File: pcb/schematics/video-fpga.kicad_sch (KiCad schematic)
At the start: 58 parts, among them J5 Conn_01x06, J6 Conn_01x06, U4 LCMXO2-7000HC-4TG144C

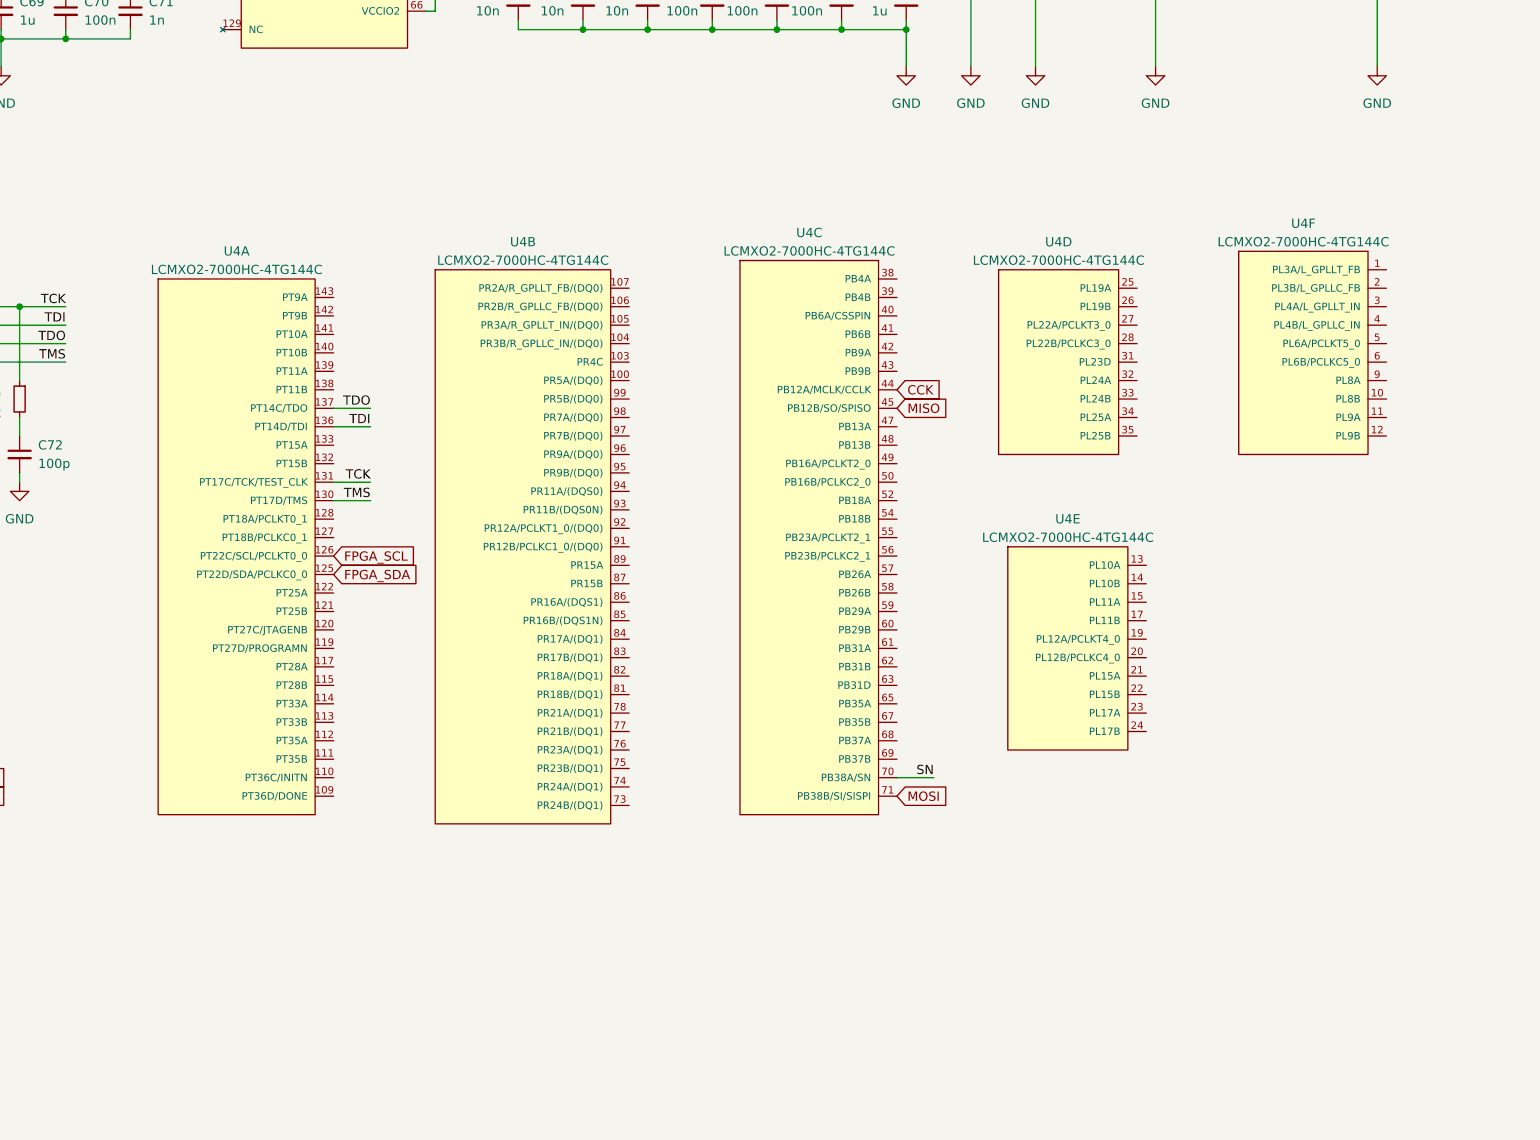
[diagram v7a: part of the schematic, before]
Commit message: add video controller oscillator
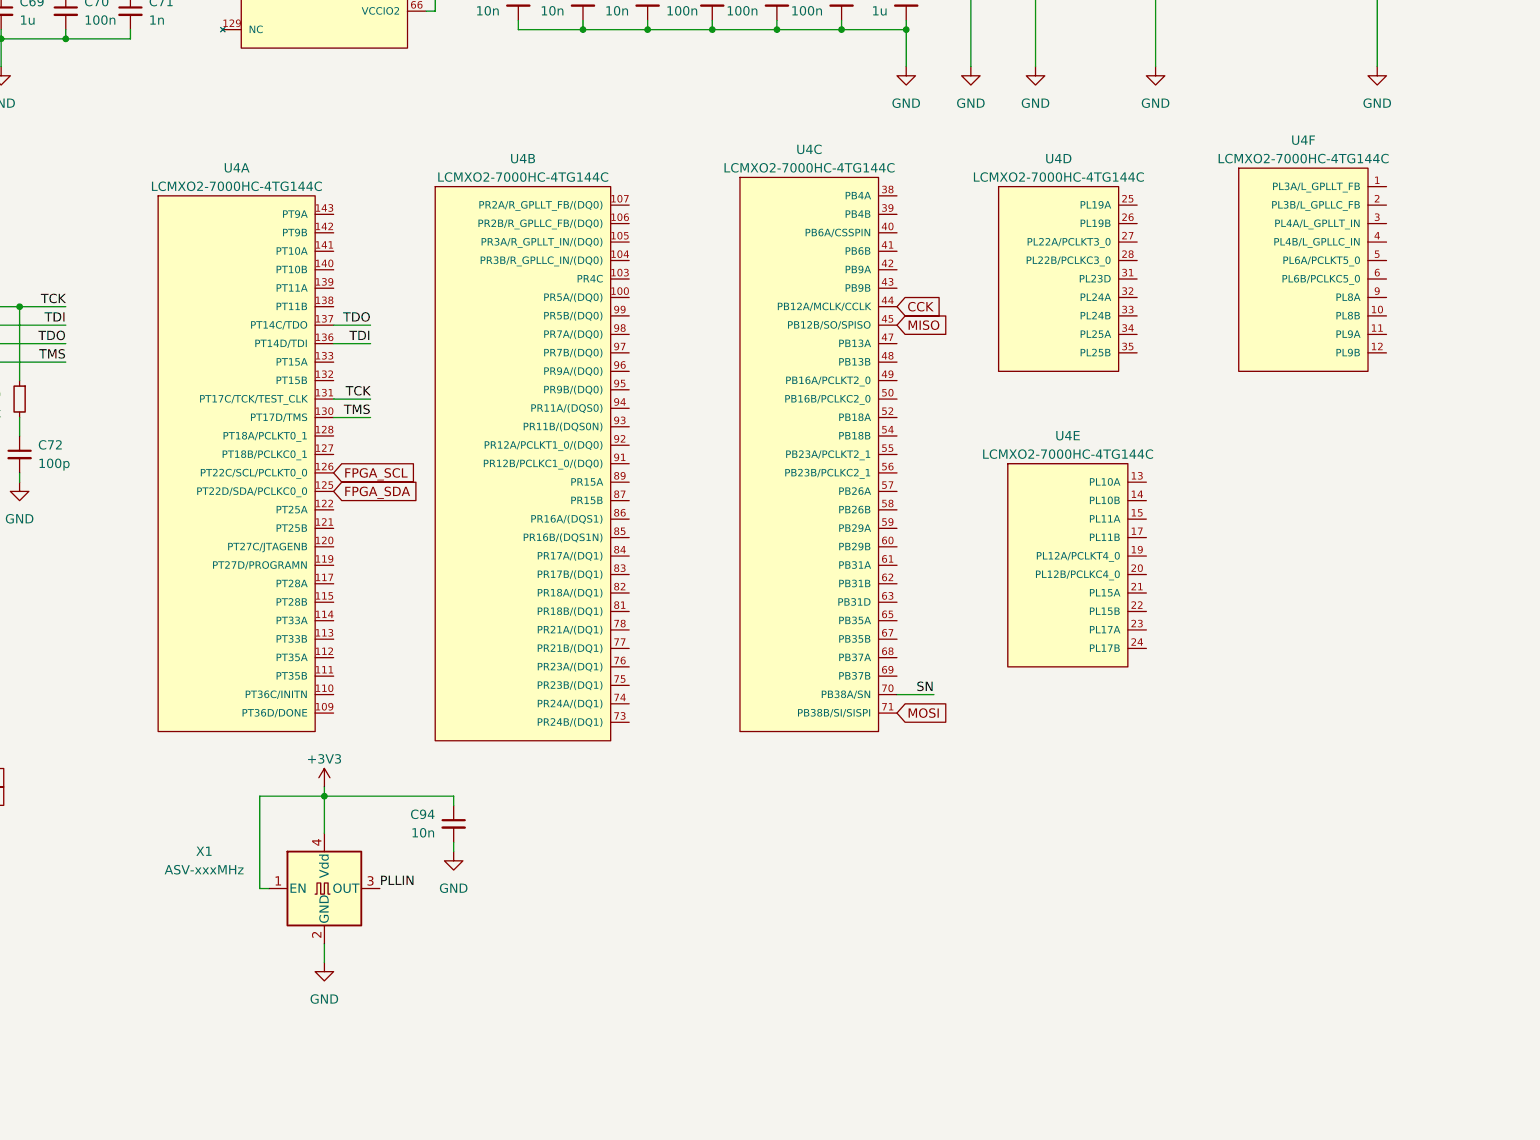
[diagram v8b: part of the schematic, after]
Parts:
- added C94: 10n, Capacitor_SMD:C_0402_1005Metric, symbol Device:C_Small
- added X1: ASV-xxxMHz, Oscillator:Oscillator_SMD_Abracon_ASV-4Pin_7.0x5.1mm, symbol Oscillator:ASV-xxxMHz
- J5, J6: footprint Connector:Tag-Connect_TC2030-IDC-FP_2x03_P1.27mm_Vertical -> Connector:Tag-Connect_TC2030-IDC-NL_2x03_P1.27mm_Vertical
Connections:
- net +3V3: now also C94.1, X1.1 (EN), X1.4 (Vdd)
- net GND: now also C94.2, X1.2 (GND)
- new net PLLIN: X1.3 (OUT)
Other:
- moved on the sheet: U4A, U4B, U4C, U4D, U4E, U4F
